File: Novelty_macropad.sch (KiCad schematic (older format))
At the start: 24 parts, among them J2 Conn_01x07, SW1 SW_Push, SW10 SW_Push, SW11 SW_Push, SW2 SW_Push, SW3 SW_Push, SW4 SW_Push, SW5 SW_Push, SW6 SW_Push, SW7 SW_Push, SW8 SW_Push, SW9 SW_Push

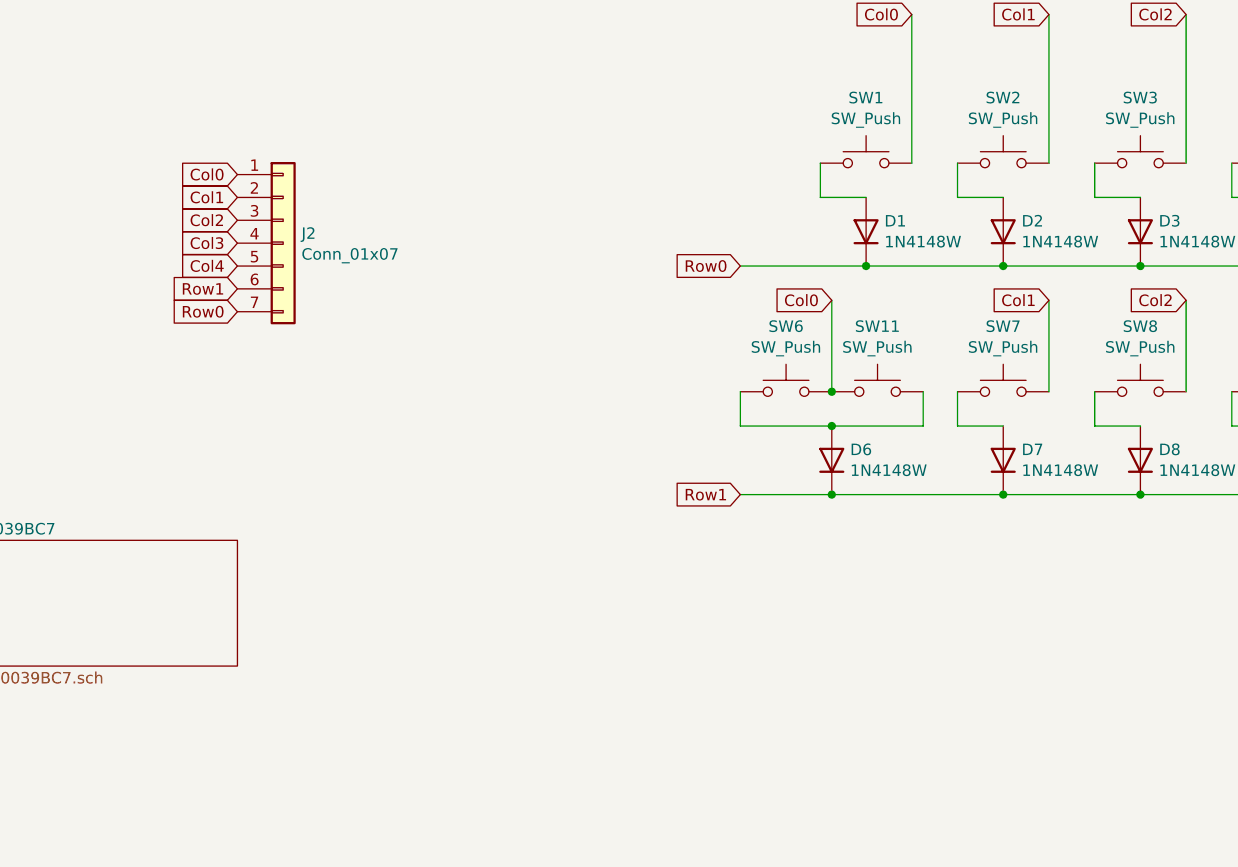
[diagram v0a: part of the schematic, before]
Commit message: plate added, step files
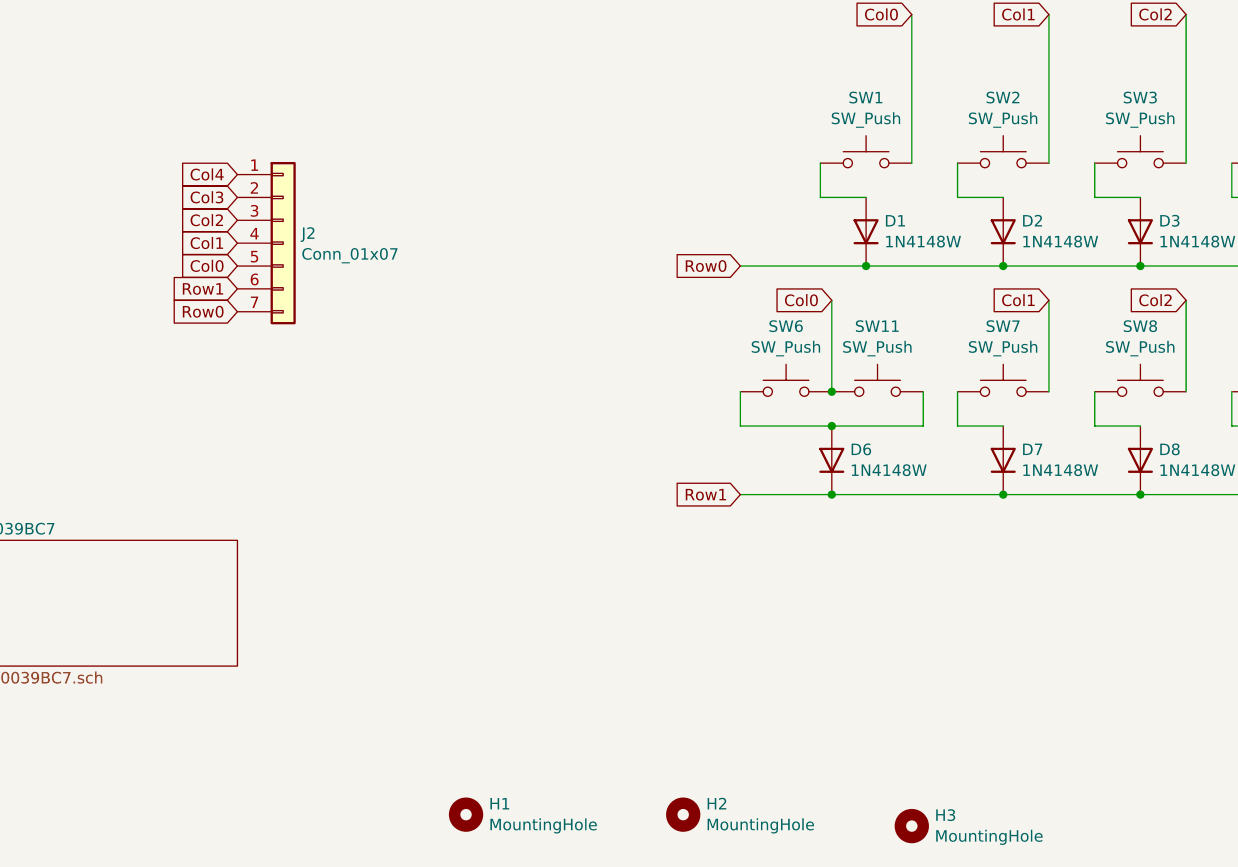
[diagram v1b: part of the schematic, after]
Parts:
- added H1, H2, H3: MountingHole, MountingHole:MountingHole_2.7mm_M2.5, symbol Mechanical:MountingHole
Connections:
- net Col0: now also J2.5 (Pin_5); no longer J2.1 (Pin_1)
- net Col1: now also J2.4 (Pin_4); no longer J2.2 (Pin_2)
- net Col3: now also J2.2 (Pin_2); no longer J2.4 (Pin_4)
- net Col4: now also J2.1 (Pin_1); no longer J2.5 (Pin_5)
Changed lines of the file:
@@
 	1    0    0    -1
 $EndComp
-Text GLabel 4500 2200 0    50   Input ~ 0
+Text GLabel 4500 2600 0    50   Input ~ 0
 Col0
-Text GLabel 4500 2300 0    50   Input ~ 0
+Text GLabel 4500 2500 0    50   Input ~ 0
 Col1
 Text GLabel 4500 2400 0    50   Input ~ 0
 Col2
-Text GLabel 4500 2500 0    50   Input ~ 0
+Text GLabel 4500 2300 0    50   Input ~ 0
 Col3
-Text GLabel 4500 2600 0    50   Input ~ 0
+Text GLabel 4500 2200 0    50   Input ~ 0
 Col4
 Text GLabel 4500 2800 0    50   Input ~ 0
@@
 F1 "file60039BC7.sch" 50
 $EndSheet
+$Comp
+L Mechanical:MountingHole H1
+U 1 1 6027E2FA
+P 5500 5000
+F 0 "H1" V 5454 5100 50  0000 L CNN
+F 1 "MountingHole" V 5545 5100 50  0000 L CNN
+F 2 "MountingHole:MountingHole_2.7mm_M2.5" H 5500 5000 50  0001 C CNN
+F 3 "~" H 5500 5000 50  0001 C CNN
+	1    5500 5000
+	0    1    1    0
+$EndComp
+$Comp
+L Mechanical:MountingHole H2
+U 1 1 6027FB83
+P 6450 5000
+F 0 "H2" V 6404 5100 50  0000 L CNN
+F 1 "MountingHole" V 6495 5100 50  0000 L CNN
+F 2 "MountingHole:MountingHole_2.7mm_M2.5" H 6450 5000 50  0001 C CNN
+F 3 "~" H 6450 5000 50  0001 C CNN
+	1    6450 5000
+	0    1    1    0
+$EndComp
+$Comp
+L Mechanical:MountingHole H3
+U 1 1 6027FE85
+P 7450 5050
+F 0 "H3" V 7404 5150 50  0000 L CNN
+F 1 "MountingHole" V 7495 5150 50  0000 L CNN
+F 2 "MountingHole:MountingHole_2.7mm_M2.5" H 7450 5050 50  0001 C CNN
+F 3 "~" H 7450 5050 50  0001 C CNN
+	1    7450 5050
+	0    1    1    0
+$EndComp
 $EndSCHEMATC

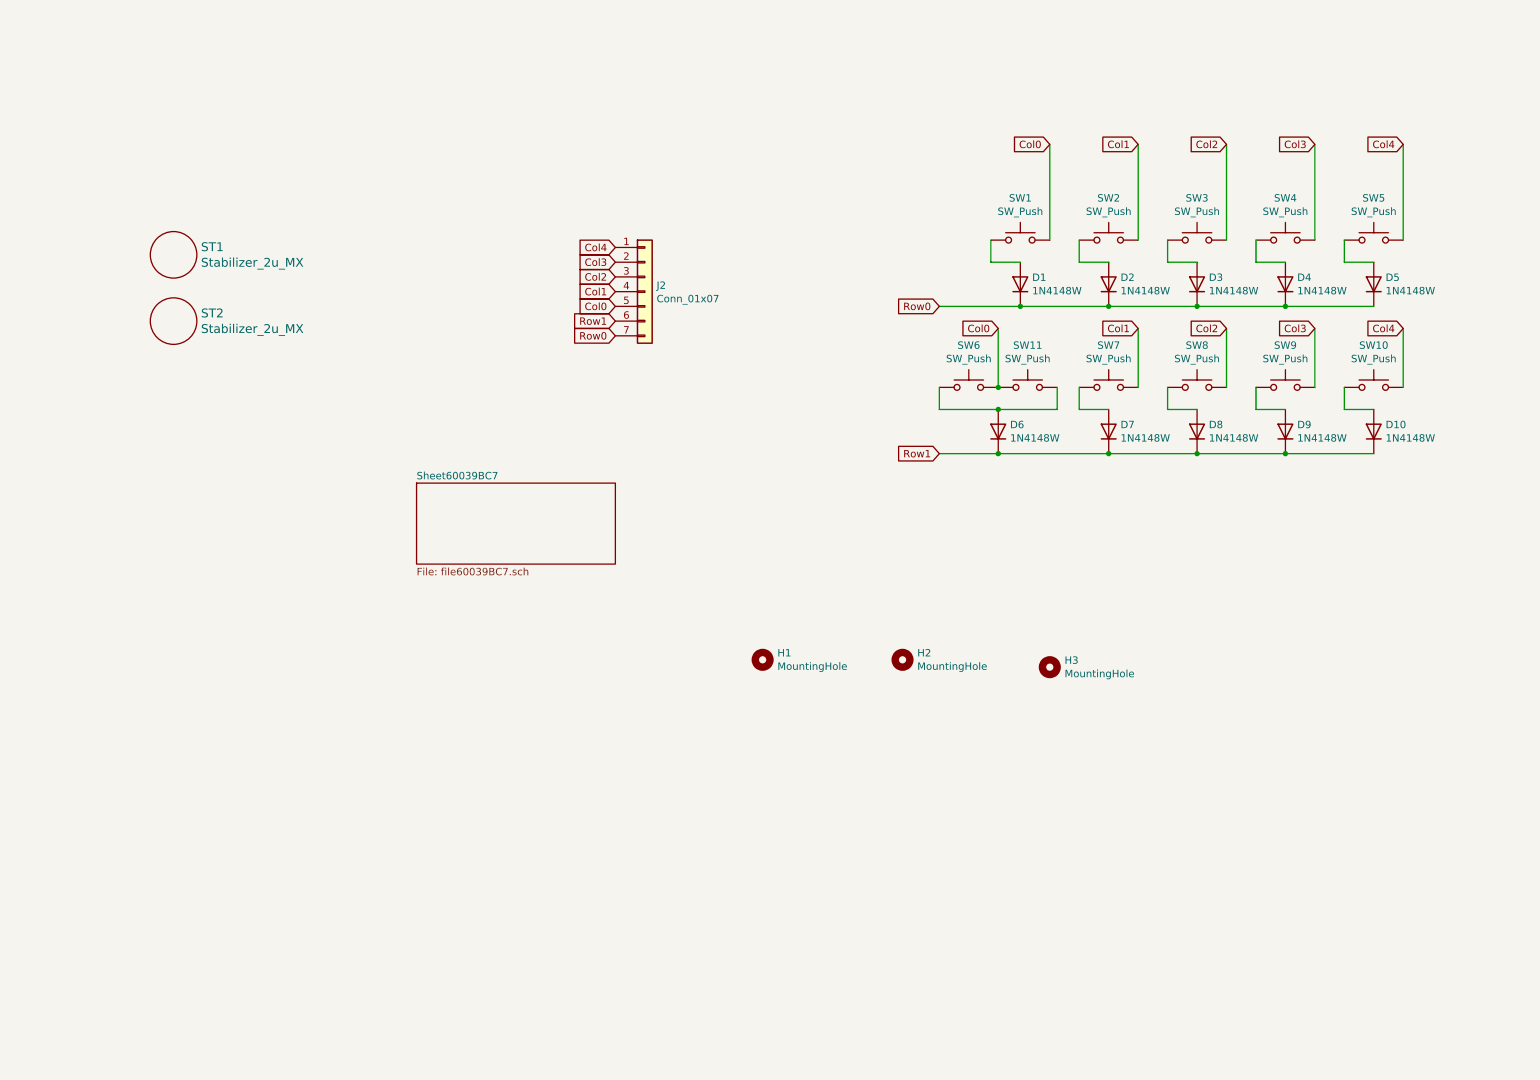
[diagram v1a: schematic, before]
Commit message: Corrected silkscreen and markings
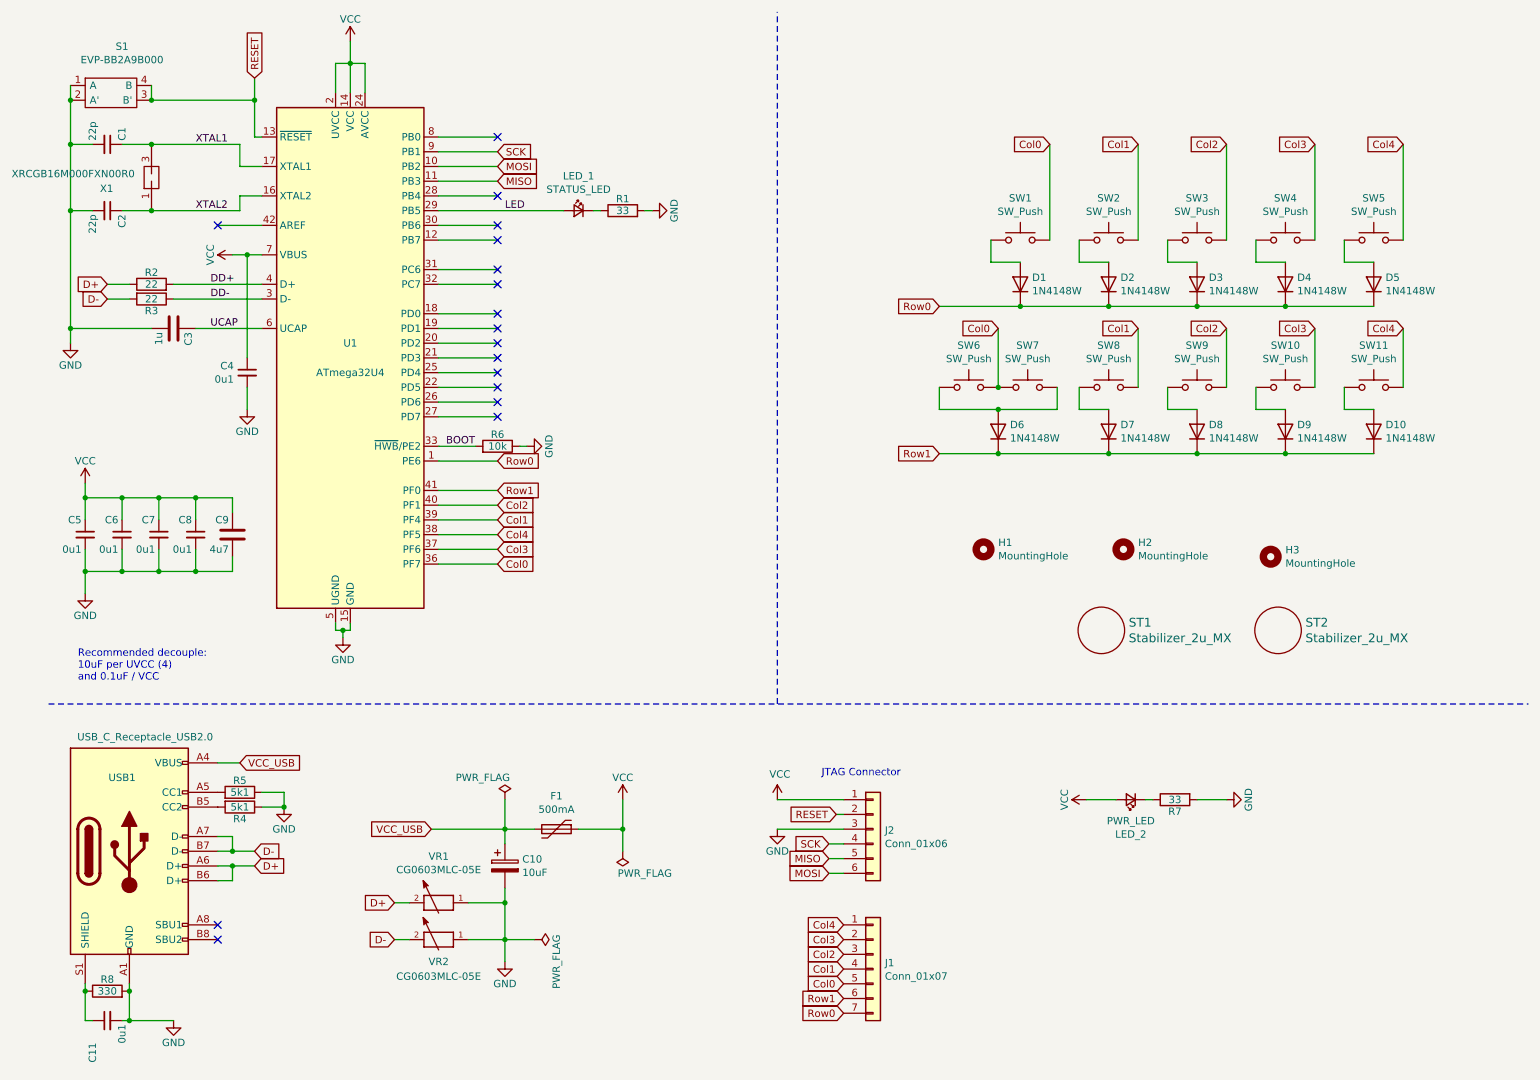
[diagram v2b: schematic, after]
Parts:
- added C1, C2: 22p, Capacitor_SMD:C_0603_1608Metric, symbol Device:C_Small
- added C10: 10uF, Capacitor_Tantalum_SMD:CP_EIA-3216-18_Kemet-A, symbol Device:CP
- added C11, C4, C5, C6, C7, C8: 0u1, Capacitor_SMD:C_0603_1608Metric, symbol Device:C_Small
- added C3: 1u, Capacitor_SMD:C_0805_2012Metric, symbol Device:C
- added C9: 4u7, Capacitor_SMD:C_0805_2012Metric, symbol Device:C
- added F1: 500mA, Fuse:Fuse_0603_1608Metric, symbol Device:Polyfuse
- added J2: Conn_01x06, Connector_PinHeader_2.54mm:PinHeader_2x03_P2.54mm_Vertical, symbol Connector_Generic:Conn_01x06
- added LED_1: STATUS_LED, LED_SMD:LED_0603_1608Metric, symbol Device:LED_Small
- added LED_2: PWR_LED, LED_SMD:LED_0603_1608Metric, symbol Device:LED_Small
- added R1, R7: 33, Resistor_SMD:R_0603_1608Metric, symbol Device:R
- added R2, R3: 22, Resistor_SMD:R_0603_1608Metric, symbol Device:R
- added R4, R5: 5k1, Resistor_SMD:R_0603_1608Metric, symbol Device:R
- added R6: 10k, Resistor_SMD:R_0603_1608Metric, symbol Device:R
- added R8: 330, Resistor_SMD:R_0603_1608Metric, symbol Device:R
- added S1: EVP-BB2A9B000, EVPBB2A9B000, symbol SamacSys_Parts:EVP-BB2A9B000
- added U1: ATmega32U4, Package_DFN_QFN:QFN-44-1EP_7x7mm_P0.5mm_EP5.15x5.15mm_ThermalVias, symbol MCU_Microchip_ATmega:ATmega32U4-AU
- added USB1: USB_C_Receptacle_USB2.0, Keyboard Library:HRO-TYPE-C-31-M-12-Assembly, symbol Connector:USB_C_Receptacle_USB2.0
- added VR1, VR2: CG0603MLC-05E, Resistor_SMD:R_0603_1608Metric, symbol Keyboard_Library:SMD-RES-VARISTOR-5V-28V(0603)
- added X1: XRCGB16M000FXN00R0, Keyboard Library:XRCGB16M000FXN1R0, symbol Keyboard_Library:XRCGB16M000FXN00R0
- renumbered J2 to J1, SW9 to SW10, SW10 to SW11, SW11 to SW7, SW7 to SW8, SW8 to SW9
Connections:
- net Col0: now also U1.36 (PF7)
- net Col1: now also U1.39 (PF4)
- net Col2: now also U1.40 (PF1)
- net Col3: now also U1.37 (PF6)
- net Col4: now also U1.38 (PF5)
- net Row0: now also U1.1 (PE6)
- net Row1: now also U1.41 (PF0)
- new net: LED_2.1 (K), R7.1
- new net: C11.1, R8.1, USB1.S1 (SHIELD)
- new net: R5.2, USB1.A5 (CC1)
- new net: R4.2, USB1.B5 (CC2)
- new net: LED_1.1 (K), R1.1
- new net BOOT: R6.2, U1.33 (~HWB~/PE2)
- new net D+: R2.1, USB1.A6 (D+), USB1.B6 (D+), VR1.2
- new net D-: R3.2, USB1.A7 (D-), USB1.B7 (D-), VR2.2
- new net DD+: R2.2, U1.4 (D+)
- new net DD-: R3.1, U1.3 (D-)
- new net GND: C1.2, C10.2, C11.2, C2.2, C3.2, C4.2, C5.2, C6.2, C7.2, C8.2, C9.2, J2.3 (Pin_3), R1.2, R4.1, R5.1, R6.1, R7.2, R8.2, S1.1 (A), S1.2 (A'), U1.15 (GND), U1.23 (GND), U1.35 (GND), U1.43 (GND), U1.5 (UGND), USB1.A1 (GND), USB1.A12 (GND), USB1.B1 (GND), USB1.B12 (GND), VR1.1, VR2.1
- new net LED: LED_1.2 (A), U1.29 (PB5)
- new net MISO: J2.5 (Pin_5), U1.11 (PB3)
- new net MOSI: J2.6 (Pin_6), U1.10 (PB2)
- new net RESET: J2.2 (Pin_2), S1.3 (B'), S1.4 (B), U1.13 (~RESET)
- new net SCK: J2.4 (Pin_4), U1.9 (PB1)
- new net UCAP: C3.1, U1.6 (UCAP)
- new net VCC: C4.1, C5.1, C6.1, C7.1, C8.1, C9.1, F1.1, J2.1 (Pin_1), LED_2.2 (A), U1.14 (VCC), U1.2 (UVCC), U1.24 (AVCC), U1.34 (VCC), U1.44 (AVCC), U1.7 (VBUS)
- new net VCC_USB: C10.1, F1.2, USB1.A4 (VBUS), USB1.A9 (VBUS), USB1.B4 (VBUS), USB1.B9 (VBUS)
- new net XTAL1: C1.1, U1.17 (XTAL1), X1.3
- new net XTAL2: C2.1, U1.16 (XTAL2), X1.1
- no-connect marks 0 -> 17
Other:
- note added: "JTAG Connector"
- note added: "Recommended decouple: \n10uF per UVCC (4)\nand 0.1uF / VCC"
- moved on the sheet: H1, H2, H3, J1, ST1, ST2
